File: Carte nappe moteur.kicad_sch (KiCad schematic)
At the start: 10 parts, among them J1 Conn_01x03_Male, J2 Conn_01x11_Male, J3 Conn_01x05_Male, J4 Conn_01x03_Male, J5 Conn_01x11_Male, J6 Conn_01x05_Male

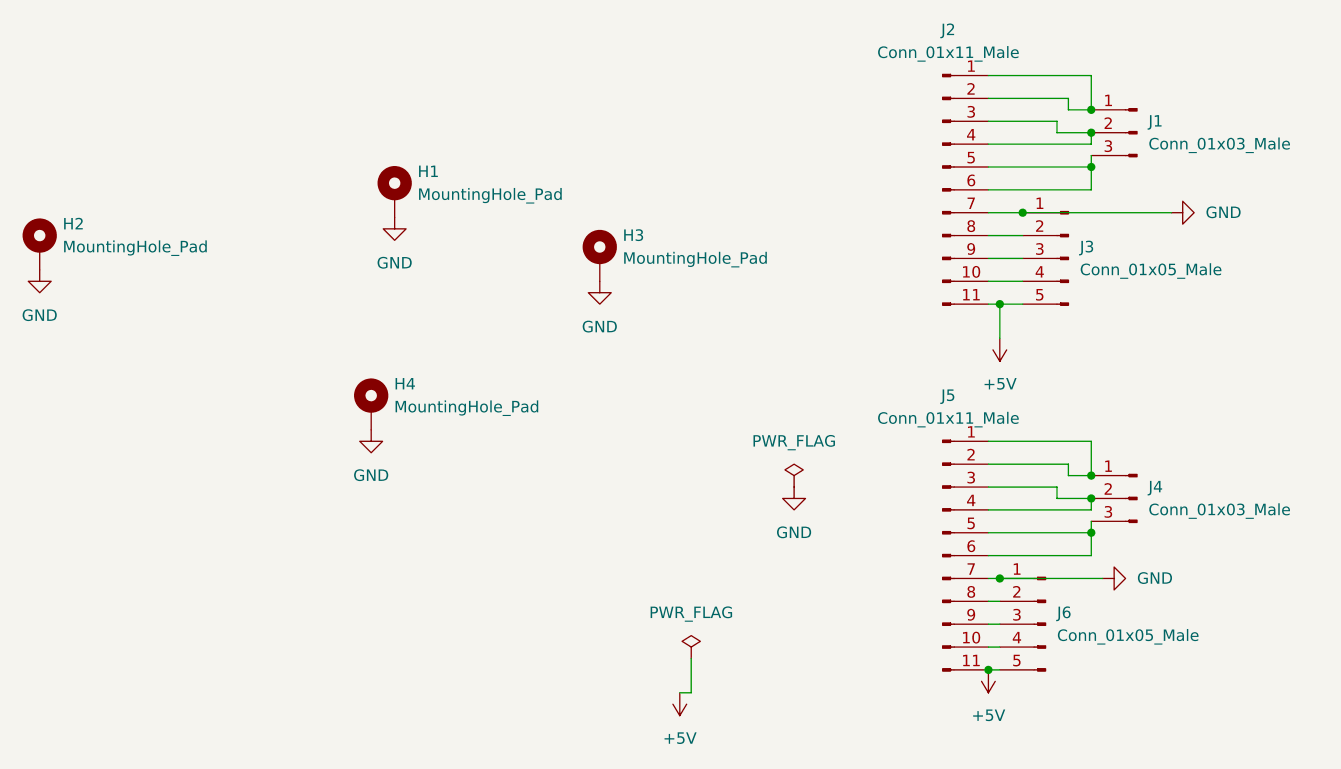
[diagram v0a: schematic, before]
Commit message: Reduction de la carte pcb
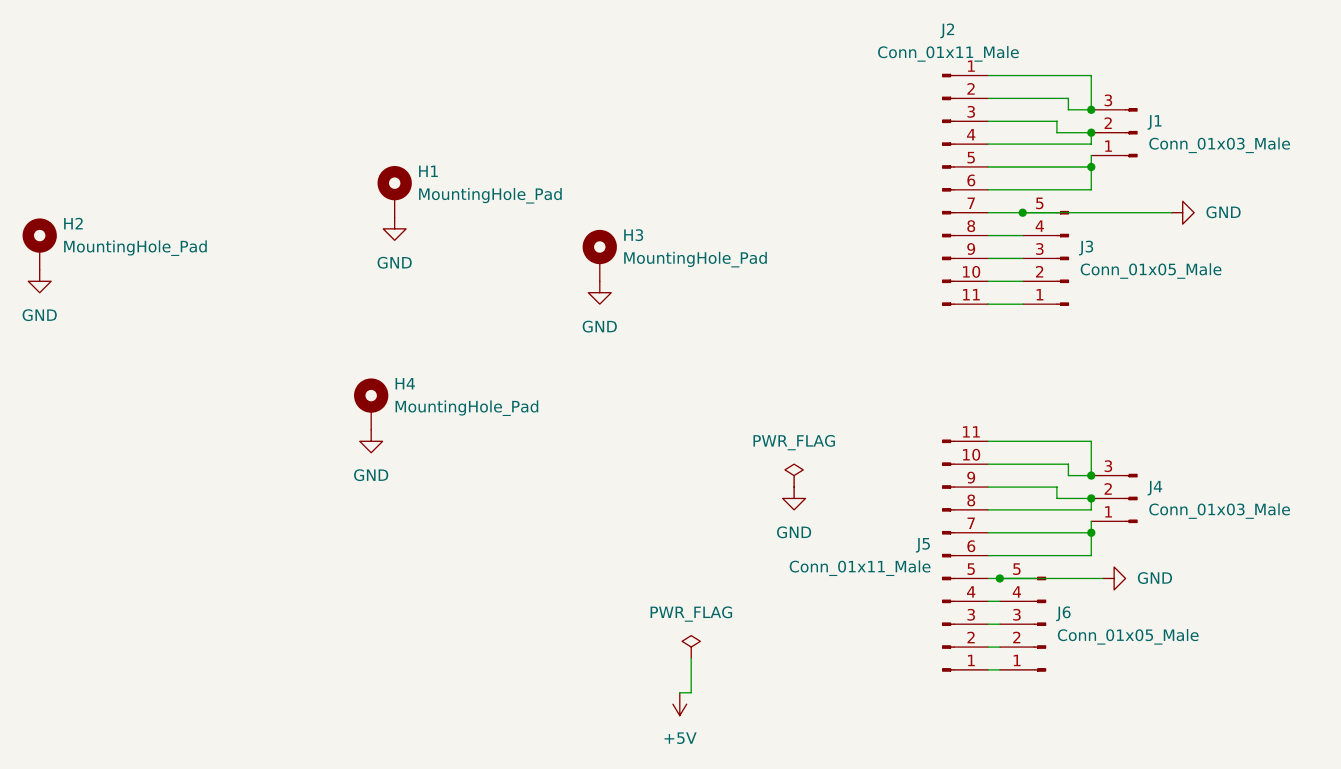
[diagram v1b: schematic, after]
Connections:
- net +5V: no longer J2.11 (Pin_11), J3.5 (Pin_5), J5.11 (Pin_11), J6.5 (Pin_5)
- net GND: now also J3.5 (Pin_5), J5.5 (Pin_5), J6.5 (Pin_5); no longer J3.1 (Pin_1), J5.7 (Pin_7), J6.1 (Pin_1)
- net at J5.10 (Pin_10): now also J4.3 (Pin_3), J5.11 (Pin_11); no longer J6.4 (Pin_4)
- net at J5.8 (Pin_8): now also J4.2 (Pin_2), J5.9 (Pin_9); no longer J6.2 (Pin_2)
- net at J6.3 (Pin_3): now also J5.3 (Pin_3); no longer J5.9 (Pin_9)
- net at J3.2 (Pin_2): now also J2.10 (Pin_10); no longer J2.8 (Pin_8)
- net at J3.4 (Pin_4): now also J2.8 (Pin_8); no longer J2.10 (Pin_10)
- net at J2.1 (Pin_1), J2.2 (Pin_2): now also J1.3 (Pin_3); no longer J1.1 (Pin_1)
- net at J2.5 (Pin_5), J2.6 (Pin_6): now also J1.1 (Pin_1); no longer J1.3 (Pin_3)
- new net: J4.1 (Pin_1), J5.6 (Pin_6), J5.7 (Pin_7)
- new net: J5.1 (Pin_1), J6.1 (Pin_1)
- new net: J5.2 (Pin_2), J6.2 (Pin_2)
- new net: J5.4 (Pin_4), J6.4 (Pin_4)
- new net: J2.11 (Pin_11), J3.1 (Pin_1)
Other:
- moved on the sheet: J1, J3, J4, J6

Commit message: Résolution problème de symétrie
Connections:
- net GND: now also J5.7 (Pin_7); no longer J5.5 (Pin_5)
- net at J5.1 (Pin_1): now also J4.1 (Pin_1), J5.2 (Pin_2); no longer J6.1 (Pin_1)
- net at J6.2 (Pin_2): now also J5.10 (Pin_10); no longer J5.2 (Pin_2)
- net at J5.3 (Pin_3): now also J4.2 (Pin_2), J5.4 (Pin_4); no longer J6.3 (Pin_3)
- net at J6.4 (Pin_4): now also J5.8 (Pin_8); no longer J5.4 (Pin_4)
- new net: J4.3 (Pin_3), J5.5 (Pin_5), J5.6 (Pin_6)
- new net: J5.11 (Pin_11), J6.1 (Pin_1)
- new net: J5.9 (Pin_9), J6.3 (Pin_3)
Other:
- moved on the sheet: J4
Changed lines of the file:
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@@
     (pin "1")
   )
-  (symbol (lib_id "Connector:Conn_01x03_Male") (at 190.5 113.03 180) (unit 1)
+  (symbol (lib_id "Connector:Conn_01x03_Male") (at 190.5 113.03 0) (mirror y) (unit 1)
     (in_bom yes) (on_board yes) (fields_autoplaced)
     (property "Reference" "J4" (id 0) (at 191.77 111.7599 0)
@@
     (pin "1")
   )
-  (symbol (lib_id "Connector:Conn_01x11_Male") (at 168.91 119.38 0) (mirror x) (unit 1)
+  (symbol (lib_id "Connector:Conn_01x11_Male") (at 168.91 119.38 0) (unit 1)
     (in_bom yes) (on_board yes) (fields_autoplaced)
-    (property "Reference" "J5" (id 0) (at 167.64 118.1099 0)
-      (effects (font (size 1.27 1.27)) (justify right))
-    )
-    (property "Value" "Conn_01x11_Male" (id 1) (at 167.64 120.6499 0)
-      (effects (font (size 1.27 1.27)) (justify right))
-    )
+    (property "Reference" "J5" (id 0) (at 169.545 101.6 0))
+    (property "Value" "Conn_01x11_Male" (id 1) (at 169.545 104.14 0))
     (property "Footprint" "Conn moteur:Molex-52610-1133" (id 2) (at 168.91 119.38 0)
       (effects (font (size 1.27 1.27)) hide)

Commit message: gitigore
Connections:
- net at J5.1 (Pin_1), J5.2 (Pin_2): now also J4.3 (Pin_3); no longer J4.1 (Pin_1)
- net at J5.5 (Pin_5), J5.6 (Pin_6): now also J4.1 (Pin_1); no longer J4.3 (Pin_3)
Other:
- moved on the sheet: J4
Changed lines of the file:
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@@
     (pin "1")
   )
-  (symbol (lib_id "Connector:Conn_01x03_Male") (at 190.5 113.03 0) (mirror y) (unit 1)
+  (symbol (lib_id "Connector:Conn_01x03_Male") (at 190.5 113.03 180) (unit 1)
     (in_bom yes) (on_board yes) (fields_autoplaced)
     (property "Reference" "J4" (id 0) (at 191.77 111.7599 0)
